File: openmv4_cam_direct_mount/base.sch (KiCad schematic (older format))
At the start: 58 parts, among them J5 XF2M-1015-1A, Q1 BSS138, Q2 Si2301BDS, U1 STM32H743VIT6, U2 OV7725, U5 TPS731XX, U8 PAM2305AABADJ, X1 MF-CON-MICROUSB-RIGHT, X2 USD-1040310811, Y1 7S-12.000MAHE-T

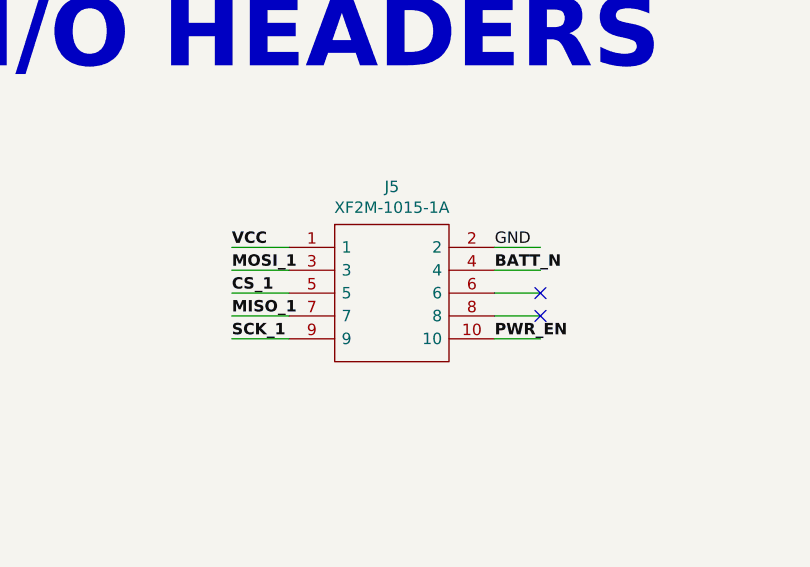
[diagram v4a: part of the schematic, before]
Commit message: Finished connecting main components
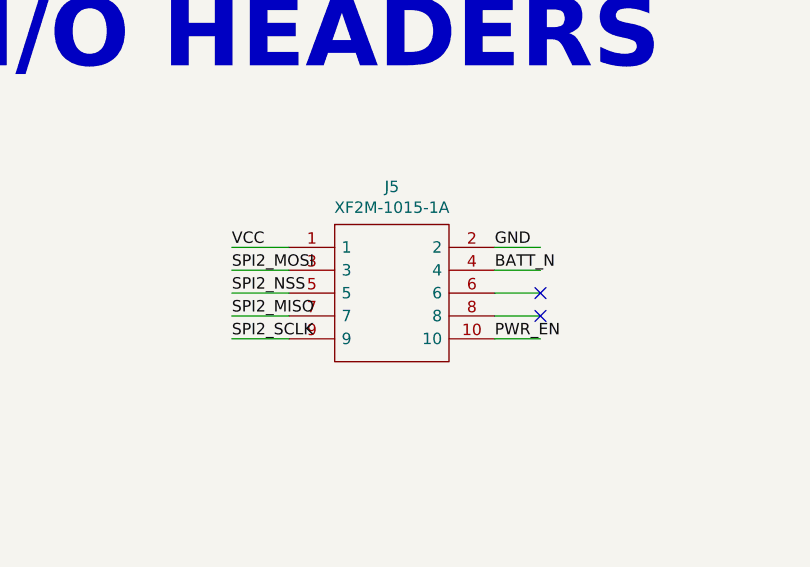
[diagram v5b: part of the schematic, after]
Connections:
- net labels removed: CS_1, MISO_1, MOSI_1, SCK_1
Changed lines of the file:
@@
 NoConn ~ 13850 2050
 NoConn ~ 13850 2150
-Text Label 13650 2250 0    50   ~ 10
+Text Label 13650 2250 0    50   ~ 0
 PWR_EN
-Text Label 12500 1850 0    50   ~ 10
+Text Label 12500 1850 0    50   ~ 0
 VCC
-Text Label 12500 1950 0    50   ~ 10
-MOSI_1
-Text Label 12500 2050 0    50   ~ 10
-CS_1
-Text Label 12500 2150 0    50   ~ 10
-MISO_1
-Text Label 12500 2250 0    50   ~ 10
-SCK_1
-Text Label 13650 1950 0    50   ~ 10
+Text Label 12500 1950 0    50   ~ 0
+SPI2_MOSI
+Text Label 12500 2050 0    50   ~ 0
+SPI2_NSS
+Text Label 12500 2150 0    50   ~ 0
+SPI2_MISO
+Text Label 12500 2250 0    50   ~ 0
+SPI2_SCLK
+Text Label 13650 1950 0    50   ~ 0
 BATT_N
 $EndSCHEMATC

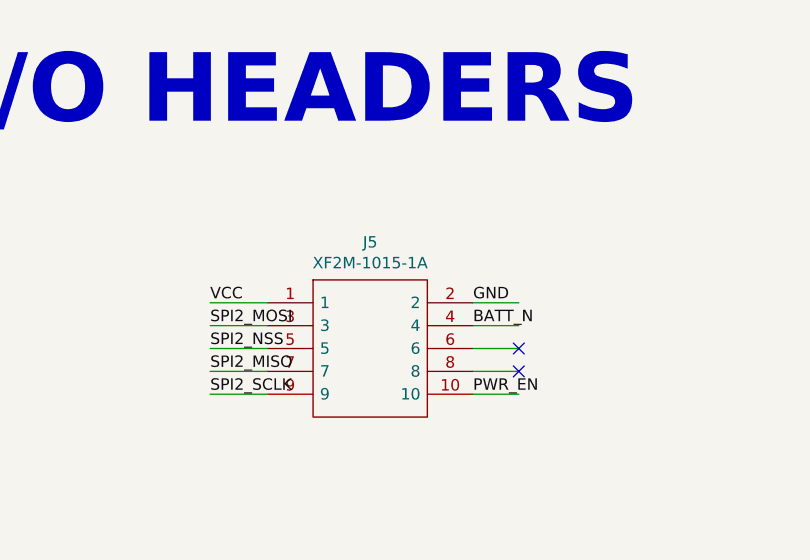
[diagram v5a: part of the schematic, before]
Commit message: Added connector
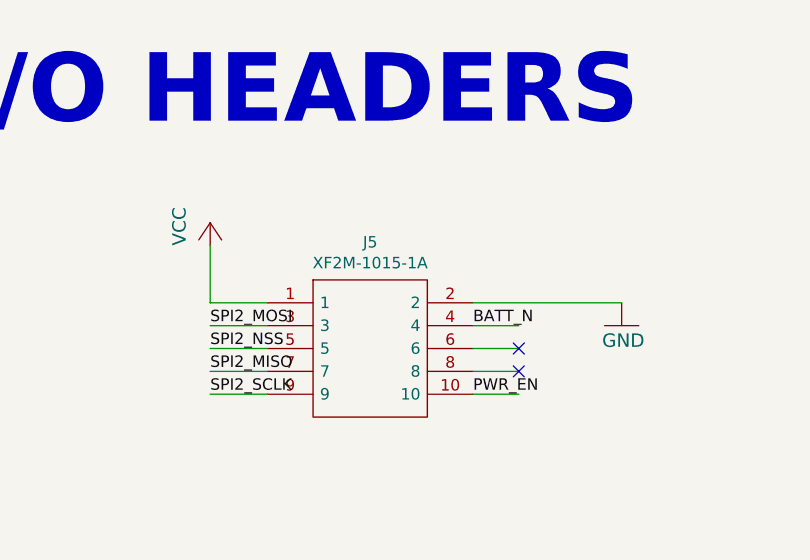
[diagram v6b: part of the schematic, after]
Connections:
- wire segments 315 -> 316
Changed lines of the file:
@@
-$EndComp
-$Comp
-L base-eagle-import:GND #GND013
-U 1 1 85B66688
-P 16100 6300
-F 0 "#GND013" H 16100 6300 50  0001 C CNN
-F 1 "GND" H 16000 6200 59  0000 L BNN
-F 2 "" H 16100 6300 50  0001 C CNN
-F 3 "" H 16100 6300 50  0001 C CNN
-	1    16100 6300
-	-1   0    0    -1
 $EndComp
 $Comp
@@
 	1    0    0    -1
 $EndComp
-Text Label 13650 1850 0    50   ~ 0
-GND
-Wire Wire Line
-	13650 1850 13850 1850
 Wire Wire Line
 	13650 1950 13850 1950
@@
 Text Label 13650 2250 0    50   ~ 0
 PWR_EN
-Text Label 12500 1850 0    50   ~ 0
-VCC
 Text Label 12500 1950 0    50   ~ 0
 SPI2_MOSI
@@
 Text Label 13650 1950 0    50   ~ 0
 BATT_N
+$Comp
+L base-eagle-import:VCC #P+?
+U 1 1 5DB9CD98
+P 12500 1500
+F 0 "#P+?" H 12500 1500 50  0001 C CNN
+F 1 "VCC" V 12400 1400 59  0000 L BNN
+F 2 "" H 12500 1500 50  0001 C CNN
+F 3 "" H 12500 1500 50  0001 C CNN
+	1    12500 1500
+	1    0    0    -1
+$EndComp
+Wire Wire Line
+	12500 1850 12500 1600
+$Comp
+L base-eagle-import:GND #GND013
+U 1 1 85B66688
+P 16100 6300
+F 0 "#GND013" H 16100 6300 50  0001 C CNN
+F 1 "GND" H 16000 6200 59  0000 L BNN
+F 2 "" H 16100 6300 50  0001 C CNN
+F 3 "" H 16100 6300 50  0001 C CNN
+	1    16100 6300
+	-1   0    0    -1
+$EndComp
+$Comp
+L base-eagle-import:GND #GND?
+U 1 1 5DBBFD41
+P 14300 1950
+F 0 "#GND?" H 14300 1950 50  0001 C CNN
+F 1 "GND" H 14200 1850 59  0000 L BNN
+F 2 "" H 14300 1950 50  0001 C CNN
+F 3 "" H 14300 1950 50  0001 C CNN
+	1    14300 1950
+	-1   0    0    -1
+$EndComp
+Wire Wire Line
+	13650 1850 14300 1850
 $EndSCHEMATC

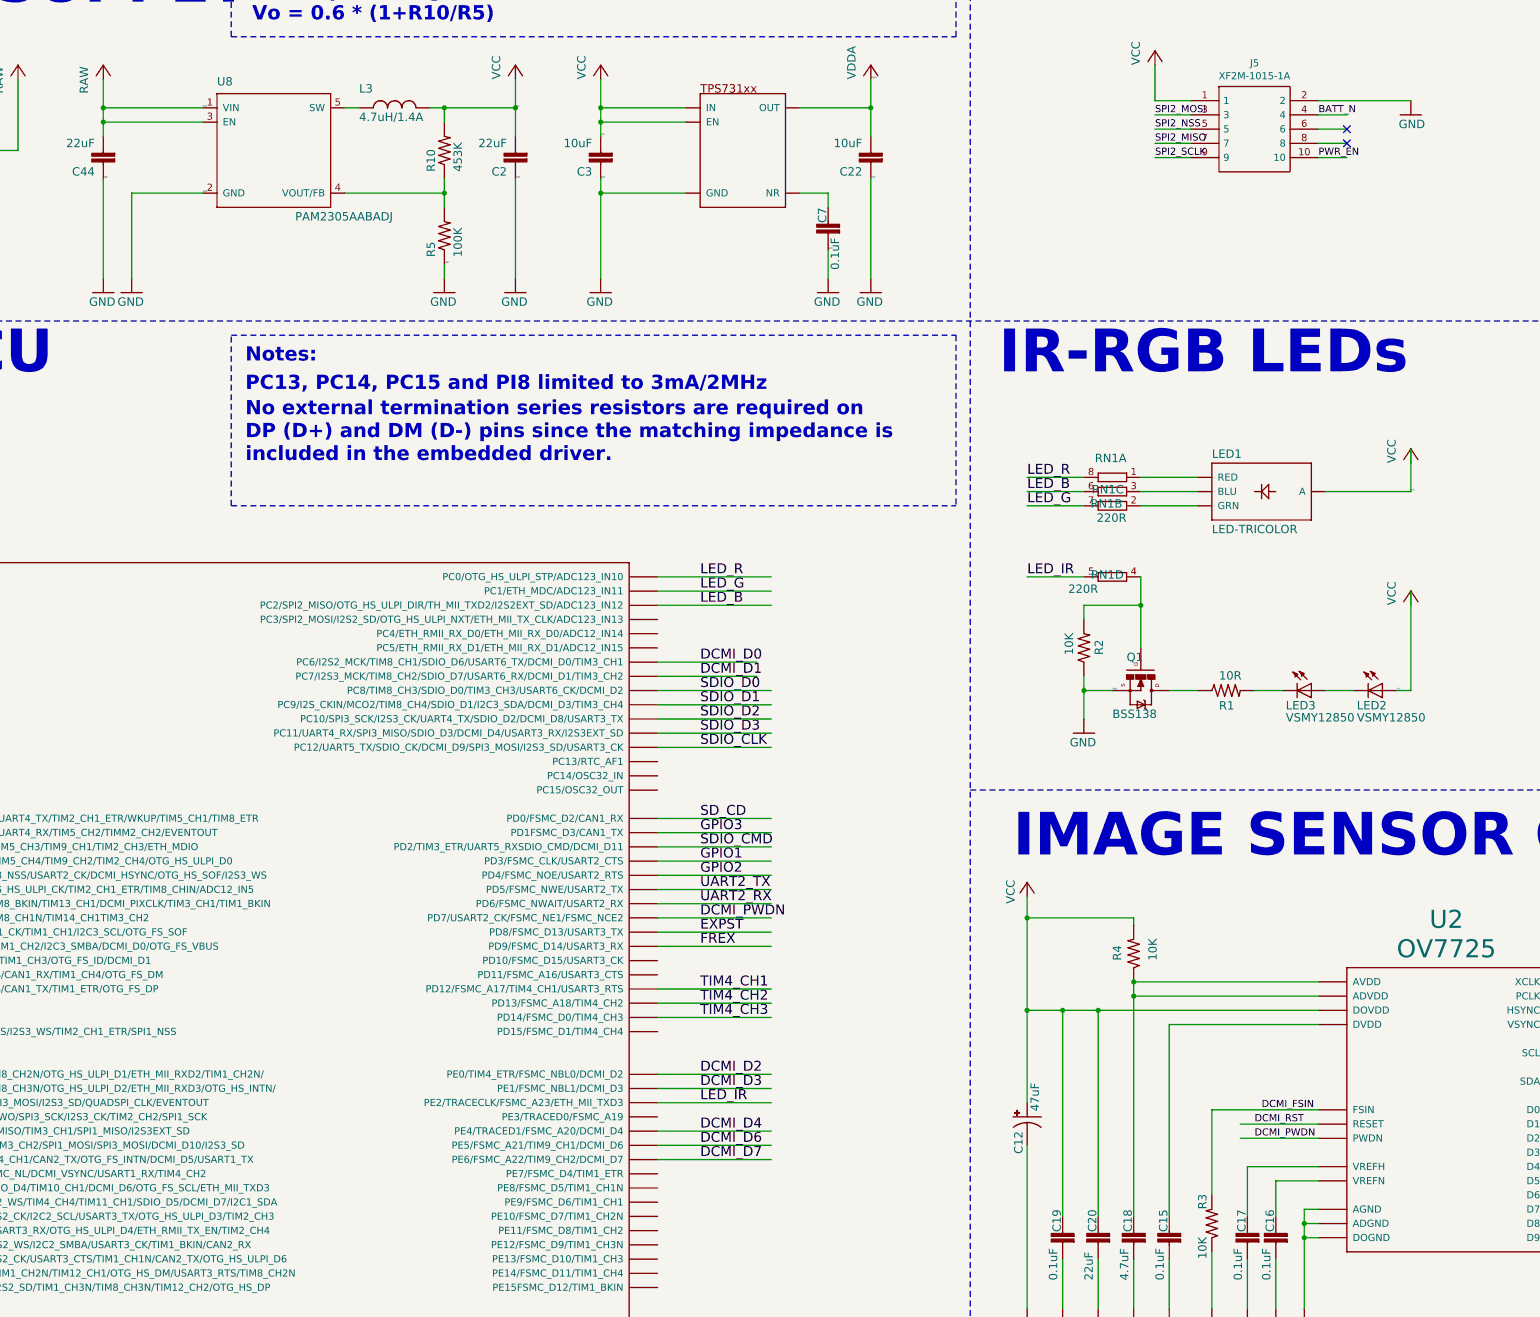
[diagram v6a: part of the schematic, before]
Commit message: Added pwr enable, fixed reg
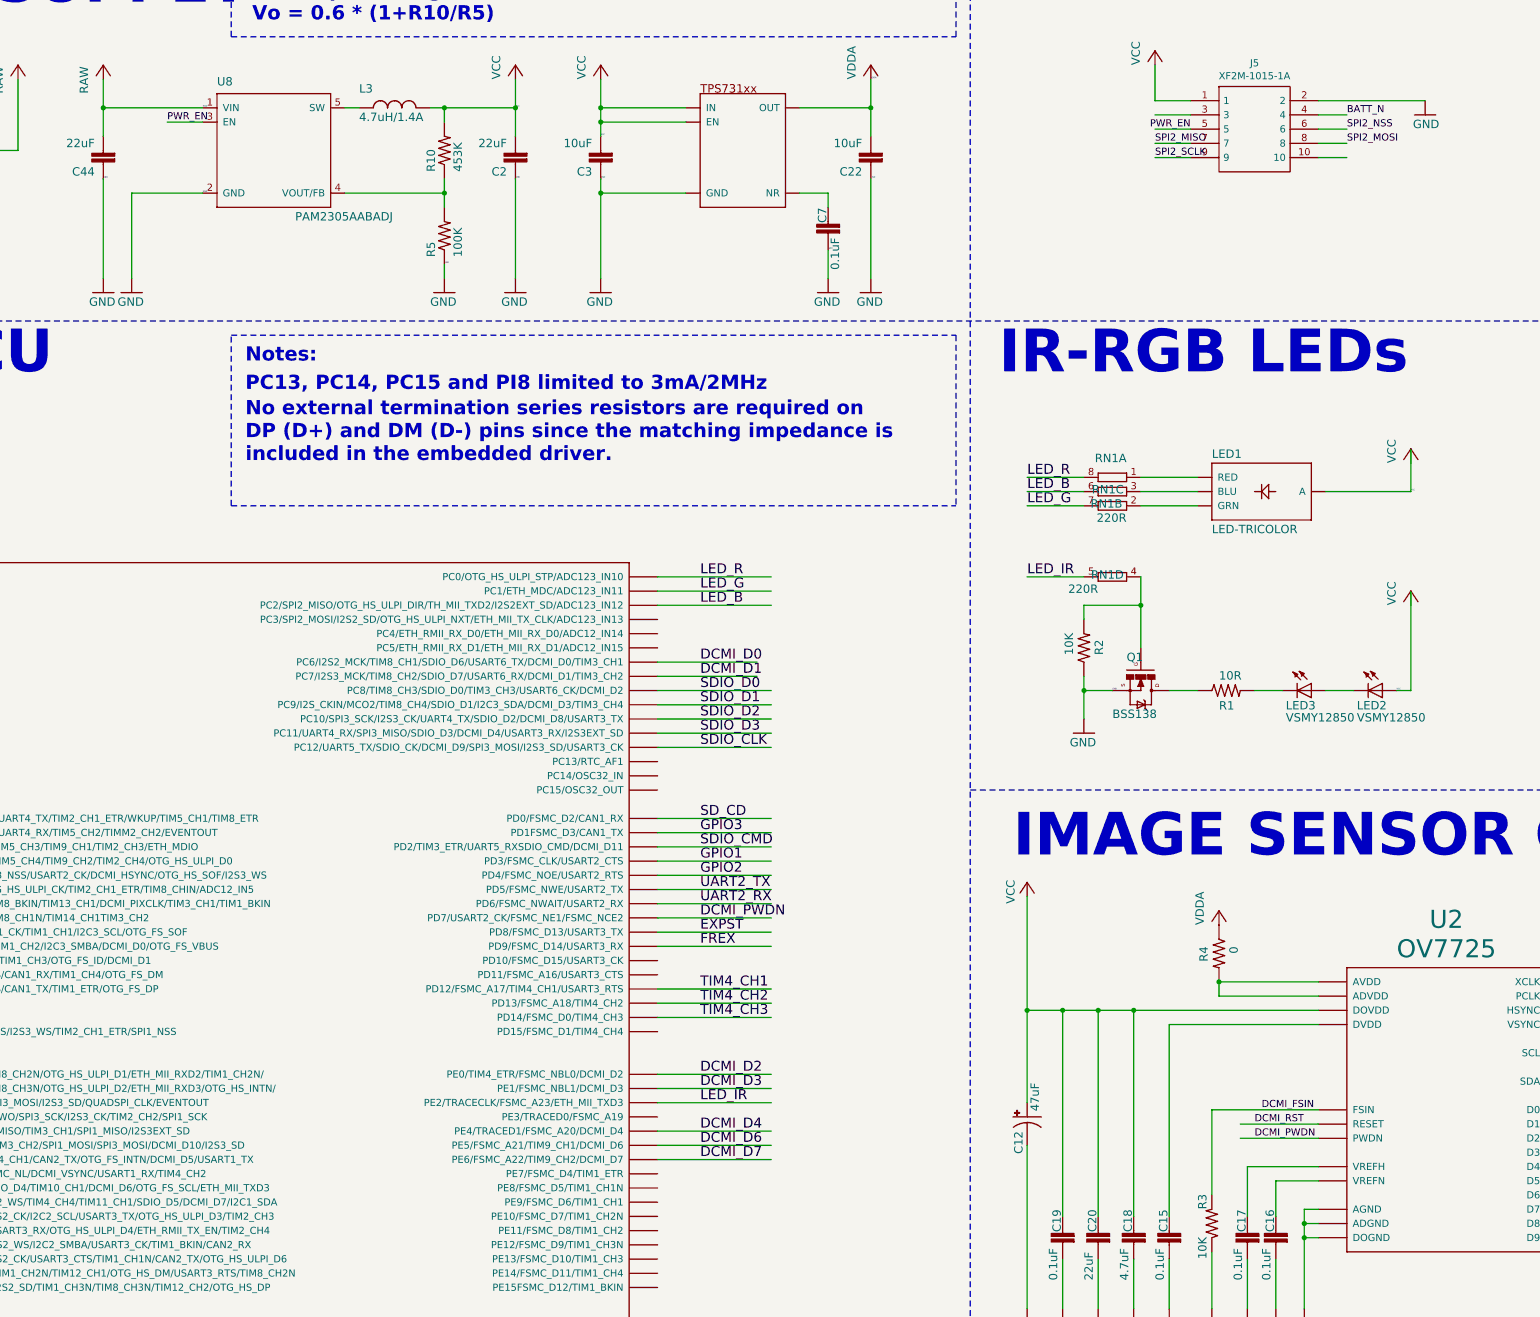
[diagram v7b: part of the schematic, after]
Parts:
- R4: value 10K -> 0; footprint openmv3:0603-RES -> base:0603-RES
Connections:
- wire segments 316 -> 313
- no-connect marks 2 -> 0
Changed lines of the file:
@@
 Wire Wire Line
 	5100 1900 5100 1700
-Wire Wire Line
-	5800 2000 5100 2000
-Wire Wire Line
-	5100 2000 5100 1900
-Wire Wire Line
-	5100 2000 5100 2100
 Connection ~ 5100 1900
-Connection ~ 5100 2000
 Text Label 5800 1900 0    10   ~ 0
 RAW
@@
 	11850 10350 11850 10000
 $Comp
-L base-eagle-import:RESISTOR0603-RES R4
-U 1 1 5E0BB5CC
-P 12350 7850
-F 0 "R4" H 12300 7700 59  0000 L BNN
-F 1 "10K" H 12300 7950 59  0000 L BNN
-F 2 "openmv3:0603-RES" H 12350 7850 50  0001 C CNN
-F 3 "" H 12350 7850 50  0001 C CNN
-	1    12350 7850
-	0    1    -1   0
-$EndComp
-Wire Wire Line
-	12350 9700 12350 8150
-$Comp
 L base-eagle-import:GND #GND0108
 U 1 1 5E0FB61A
@@
 $EndComp
 Wire Wire Line
-	13650 8250 12100 8250
+	13650 8250 12350 8250
 Connection ~ 11600 8250
 Wire Wire Line
@@
 Wire Wire Line
 	12100 8250 11850 8250
-Wire Wire Line
-	13650 8150 12350 8150
-Connection ~ 12350 8150
-Wire Wire Line
-	13650 8050 12350 8050
-Connection ~ 12350 8050
-Wire Wire Line
-	12350 7650 12350 7600
-Wire Wire Line
-	12350 7600 11600 7600
-Wire Wire Line
-	11600 7600 11600 8250
-Wire Wire Line
-	11600 7600 11600 7450
-Wire Wire Line
-	12350 8050 12350 8150
-Connection ~ 11600 7600
 $Comp
 L openmv3-eagle-import:LENSMOUNT20MM LM1
@@
 Wire Wire Line
 	12750 1850 12500 1850
-NoConn ~ 13850 2050
-NoConn ~ 13850 2150
-Text Label 13650 2250 0    50   ~ 0
+Text Label 12750 2050 2    50   ~ 0
 PWR_EN
-Text Label 12500 1950 0    50   ~ 0
+Text Label 13850 2150 0    50   ~ 0
 SPI2_MOSI
-Text Label 12500 2050 0    50   ~ 0
+Text Label 13850 2050 0    50   ~ 0
 SPI2_NSS
 Text Label 12500 2150 0    50   ~ 0
@@
 Text Label 12500 2250 0    50   ~ 0
 SPI2_SCLK
-Text Label 13650 1950 0    50   ~ 0
+Text Label 13850 1950 0    50   ~ 0
 BATT_N
 $Comp
-L base-eagle-import:VCC #P+?
+L base-eagle-import:VCC #P+0102
 U 1 1 5DB9CD98
 P 12500 1500
-F 0 "#P+?" H 12500 1500 50  0001 C CNN
+F 0 "#P+0102" H 12500 1500 50  0001 C CNN
 F 1 "VCC" V 12400 1400 59  0000 L BNN
 F 2 "" H 12500 1500 50  0001 C CNN
@@
 	-1   0    0    -1
 $EndComp
-$Comp
-L base-eagle-import:GND #GND?
+Wire Wire Line
+	13650 1850 14400 1850
+$Comp
+L base-eagle-import:GND #GND0109
 U 1 1 5DBBFD41
-P 14300 1950
-F 0 "#GND?" H 14300 1950 50  0001 C CNN
-F 1 "GND" H 14200 1850 59  0000 L BNN
-F 2 "" H 14300 1950 50  0001 C CNN
-F 3 "" H 14300 1950 50  0001 C CNN
-	1    14300 1950
-	-1   0    0    -1
-$EndComp
-Wire Wire Line
-	13650 1850 14300 1850
+P 14400 1950
+F 0 "#GND0109" H 14400 1950 50  0001 C CNN
+F 1 "GND" H 14300 1850 59  0000 L BNN
+F 2 "" H 14400 1950 50  0001 C CNN
+F 3 "" H 14400 1950 50  0001 C CNN
+	1    14400 1950
+	-1   0    0    -1
+$EndComp
+Wire Wire Line
+	11600 7450 11600 8250
+Wire Wire Line
+	12350 8250 12350 9700
+Connection ~ 12350 8250
+Wire Wire Line
+	12350 8250 12100 8250
+$Comp
+L base-eagle-import:VDDA #VDDA0101
+U 1 1 5DB943C2
+P 12950 7650
+F 0 "#VDDA0101" H 12950 7650 50  0001 C CNN
+F 1 "VDDA" V 12850 7650 59  0000 L BNN
+F 2 "" H 12950 7650 50  0001 C CNN
+F 3 "" H 12950 7650 50  0001 C CNN
+	1    12950 7650
+	1    0    0    -1
+$EndComp
+Wire Wire Line
+	13650 8050 12950 8050
+Wire Wire Line
+	13650 8150 12950 8150
+Connection ~ 12950 8050
+Wire Wire Line
+	12950 8050 12950 8150
+Wire Wire Line
+	5100 1900 5100 2100
+Text Label 5550 2000 0    50   ~ 0
+PWR_EN
+Wire Wire Line
+	5800 2000 5550 2000
+$Comp
+L base-eagle-import:RESISTOR0603-RES R4
+U 1 1 5DB4BD49
+P 12950 7850
+F 0 "R4" H 12900 7709 59  0000 L BNN
+F 1 "0" H 12900 7920 59  0000 L BNN
+F 2 "base:0603-RES" H 12950 7850 50  0001 C CNN
+F 3 "" H 12950 7850 50  0001 C CNN
+	1    12950 7850
+	0    1    1    0
+$EndComp
 $EndSCHEMATC

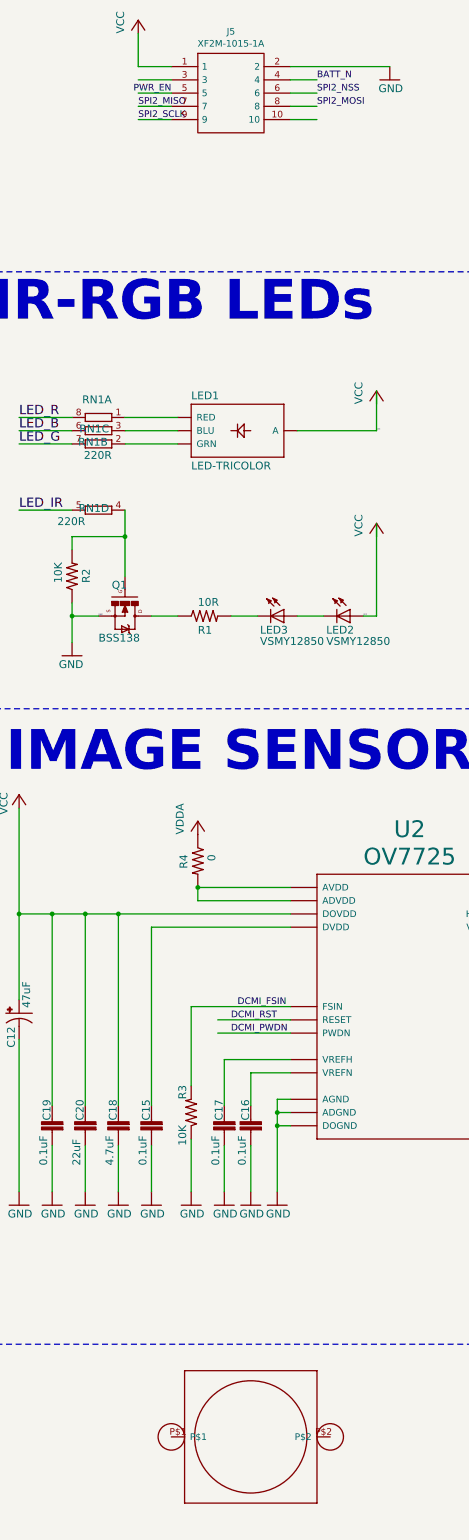
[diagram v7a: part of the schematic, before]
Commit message: Fixed clearance issue
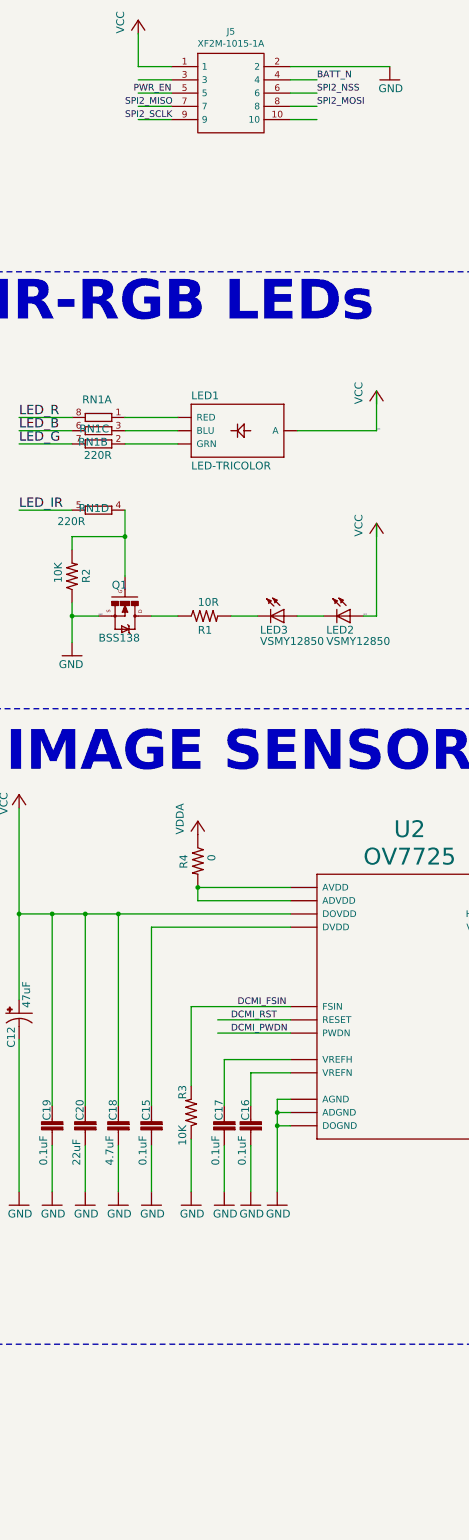
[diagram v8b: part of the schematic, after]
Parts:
- removed LM1: LENSMOUNT20MM, openmv3:LENSMOUNT-20MM, symbol openmv3-eagle-import:LENSMOUNT20MM
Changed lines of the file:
@@
 	12100 8250 11850 8250
-$Comp
-L openmv3-eagle-import:LENSMOUNT20MM LM1
-U 1 1 5DAA9666
-P 13350 12200
-F 0 "LM1" H 13400 12250 50  0001 C CNN
-F 1 "LENSMOUNT20MM" H 13350 12200 50  0001 C CNN
-F 2 "openmv3:LENSMOUNT-20MM" H 13350 12200 50  0001 C CNN
-F 3 "" H 13350 12200 50  0001 C CNN
-	1    13350 12200
-	1    0    0    -1
-$EndComp
 $Comp
 L base-eagle-import:DINA3_L #FRAME1
@@
 Text Label 13850 2050 0    50   ~ 0
 SPI2_NSS
-Text Label 12500 2150 0    50   ~ 0
+Text Label 12400 2150 0    50   ~ 0
 SPI2_MISO
-Text Label 12500 2250 0    50   ~ 0
+Text Label 12400 2250 0    50   ~ 0
 SPI2_SCLK
 Text Label 13850 1950 0    50   ~ 0
